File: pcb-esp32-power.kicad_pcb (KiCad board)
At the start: 2 copper layers, 48.6 x 47.4 mm, 35 parts, among them IC1 IP5108, IC2 SY8008B, J1 C-OBD-II-16M, J2 Conn_01x02, J3 Bus_Connector, U1 STEPDOWN12_5

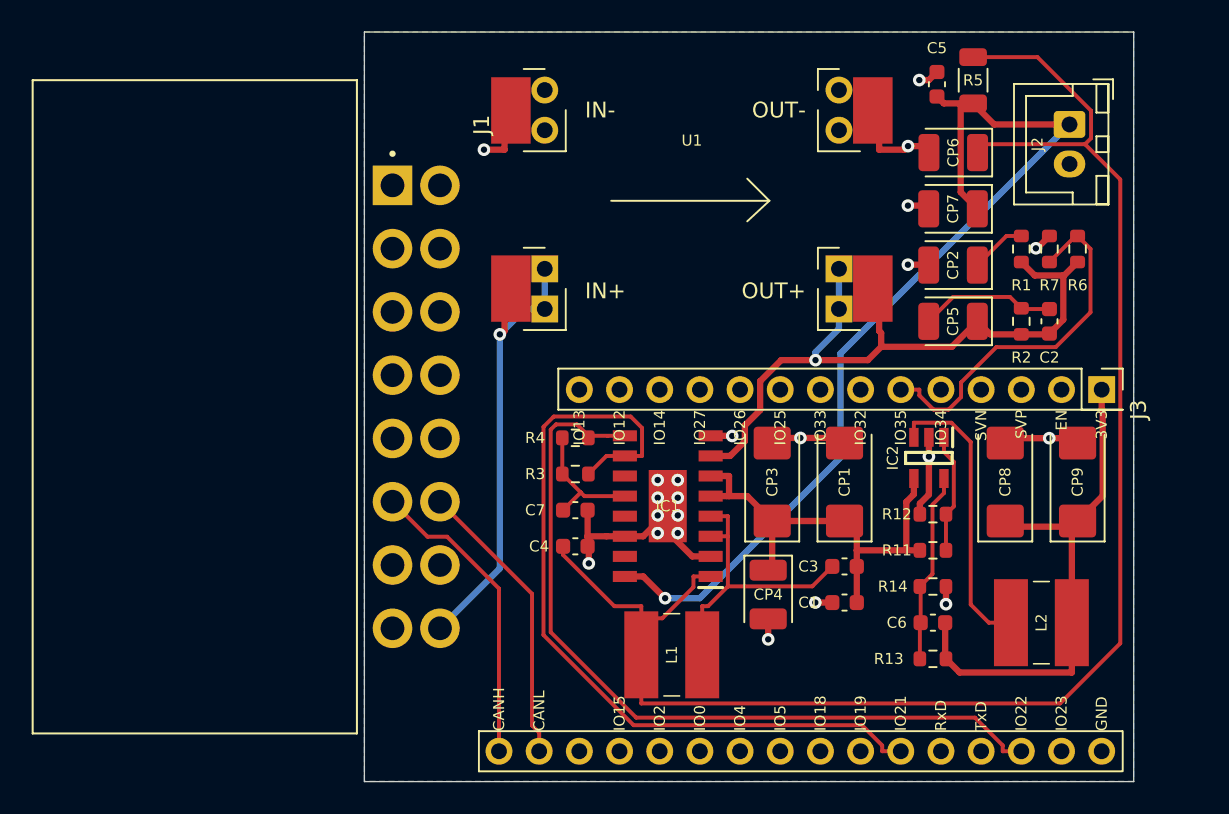
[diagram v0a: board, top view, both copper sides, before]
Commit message: Footprints für "Hand solder"
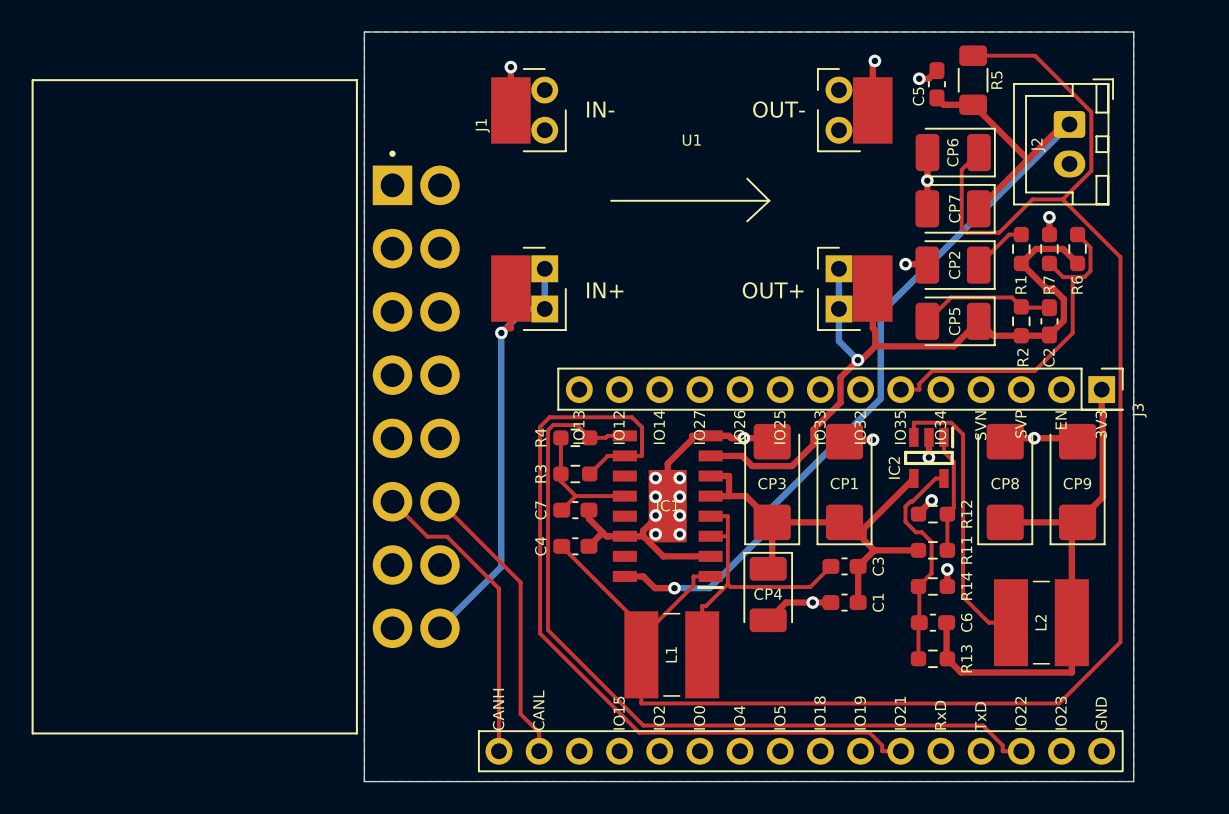
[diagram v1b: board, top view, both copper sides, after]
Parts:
- C1, C2, C3, C4, C5, C6, C7: footprint Capacitor_SMD:C_0603_1608Metric -> Capacitor_SMD:C_0603_1608Metric_Pad1.08x0.95mm_HandSolder
- CP1, CP3, CP8, CP9: footprint Capacitor_Tantalum_SMD:CP_EIA-6032-28_Kemet-C -> Capacitor_Tantalum_SMD:CP_EIA-6032-28_Kemet-C_Pad2.25x2.35mm_HandSolder
- CP2, CP4, CP5, CP6, CP7: footprint Capacitor_Tantalum_SMD:CP_EIA-3528-21_Kemet-B -> Capacitor_Tantalum_SMD:CP_EIA-3528-21_Kemet-B_Pad1.50x2.35mm_HandSolder
- R1, R11, R12, R13, R14, R2, R3, R4, R6, R7: footprint Resistor_SMD:R_0603_1608Metric -> Resistor_SMD:R_0603_1608Metric_Pad0.98x0.95mm_HandSolder
- R5: footprint Resistor_SMD:R_1206_3216Metric -> Resistor_SMD:R_1206_3216Metric_Pad1.30x1.75mm_HandSolder
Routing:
- net Net-(C4-Pad1): track 101.3 -> 107.3 mm
- net GND: track 48.3 -> 51.2 mm, vias 22 -> 21
- net 5VIN: track 45.2 -> 47.9 mm
- net Net-(C6-Pad2): track 12.1 -> 14.1 mm
- net EXTPOW: track 23.4 -> 21.9 mm
- net +BATT: track 61.2 -> 59.7 mm
- net +12V: track 29.1 -> 29.7 mm

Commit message: Mit SY8008
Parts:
- removed C1, C4, C5: 104, Capacitor_SMD:C_0603_1608Metric_Pad1.08x0.95mm_HandSolder
- removed C6: 47pF, Capacitor_SMD:C_0603_1608Metric_Pad1.08x0.95mm_HandSolder
- removed C7: 2.2uF, Capacitor_SMD:C_0603_1608Metric_Pad1.08x0.95mm_HandSolder
- removed CP6, CP7: 10uF, Capacitor_Tantalum_SMD:CP_EIA-3528-21_Kemet-B_Pad1.50x2.35mm_HandSolder
- removed CP8, CP9: 22uF, Capacitor_Tantalum_SMD:CP_EIA-6032-28_Kemet-C_Pad2.25x2.35mm_HandSolder
- removed L2: 2.2uH, IP5108:CD54_Inductor
- removed the R1 at (167.9, 100.3)
- removed R11, R12: 100k, Resistor_SMD:R_0603_1608Metric_Pad0.98x0.95mm_HandSolder
- removed R13: 453k 1%, Resistor_SMD:R_0603_1608Metric_Pad0.98x0.95mm_HandSolder
- removed R14: 100k 1%, Resistor_SMD:R_0603_1608Metric_Pad0.98x0.95mm_HandSolder
- removed the R2 at (167.9, 104.9)
- added D1: B5819W, Diode_SMD:D_SOD-123, F.Cu at (157.2, 117.6)
- added Q1: Si2307BDS, Package_TO_SOT_SMD:SOT-23, F.Cu at (157.2, 114.0)
- added R10: 100k 1%, Resistor_SMD:R_0603_1608Metric_Pad0.98x0.95mm_HandSolder, F.Cu at (162.6, 122.7)
- added R6: 10K, Resistor_SMD:R_0603_1608Metric_Pad0.98x0.95mm_HandSolder, F.Cu at (157.7, 127.3)
- added R7: 100k, Resistor_SMD:R_0603_1608Metric_Pad0.98x0.95mm_HandSolder, F.Cu at (162.6, 120.4)
- added R8: 100k, Resistor_SMD:R_0603_1608Metric_Pad0.98x0.95mm_HandSolder, F.Cu at (162.6, 118.1)
- added R9: 453k 1%, Resistor_SMD:R_0603_1608Metric_Pad0.98x0.95mm_HandSolder, F.Cu at (162.6, 127.3)
- C2: value 104 -> 100nF
- C3: value 4.7nF -> 47pF
- CP2, CP5: value 10uF -> 22uF; footprint Capacitor_Tantalum_SMD:CP_EIA-3528-21_Kemet-B_Pad1.50x2.35mm_HandSolder -> Capacitor_Tantalum_SMD:CP_EIA-6032-28_Kemet-C_Pad2.25x2.35mm_HandSolder
- CP3: value 22uF -> 10uF; footprint Capacitor_Tantalum_SMD:CP_EIA-6032-28_Kemet-C_Pad2.25x2.35mm_HandSolder -> Capacitor_Tantalum_SMD:CP_EIA-3528-21_Kemet-B_Pad1.50x2.35mm_HandSolder
- IC1: value IP5108 -> TP4054-42-SOT25-R; footprint IP5108:IP5108 -> tp4054:SOT95P280X100-5N
- L1: value 1uH -> 2.2uH
- R1: renamed from R6; value R -> 200k
- R2: renamed from R7; value R -> 390k
- R3, R4: value 3.3k -> 470k
- R5: value 10mOhm -> 2K; footprint Resistor_SMD:R_1206_3216Metric_Pad1.30x1.75mm_HandSolder -> Resistor_SMD:R_0603_1608Metric_Pad0.98x0.95mm_HandSolder
- moved IC1 30.7 mm to (171.7, 100.6), turned to 270 degrees
- moved R4 26.1 mm to (164.8, 105.2), turned to 90 degrees
- moved CP4 25.9 mm to (163.6, 99.1), turned to 90 degrees
- moved CP3 25.3 mm to (163.6, 92.5), turned to 270 degrees
- moved R3 25.0 mm to (162.8, 105.2), turned to 270 degrees
- moved L1 23.9 mm to (169.7, 124.2), turned to 270 degrees
- moved C2 23.3 mm to (157.7, 125.0), turned to 180 degrees
- moved CP5 18.3 mm to (155.7, 121.4)
- moved R5 17.5 mm to (173.0, 105.2), turned to 270 degrees
- moved CP2 16.9 mm to (172.0, 116.1), turned to 90 degrees
- moved CP1 11.0 mm to (167.6, 116.1)
- moved C3 7.42 mm to (162.6, 125.0)
- moved R2 5.58 mm to (166.9, 105.2)
- moved R1 5.45 mm to (168.9, 105.2), turned to 270 degrees
- moved IC2 0.92 mm to (162.6, 114.3)
- renumbered J3 to J2, J2 to J3
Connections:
- C2 pad 1: 5VIN -> 5VOUT
- C2 pad 2: Net-(C2-Pad2) -> GND
- C3 pad 1: 5VOUT -> +3V3
- CP1 pad 1: 5VOUT -> +3V3
- CP2 pad 1: Net-(CP2-Pad1) -> +3V3
- CP3 pad 1: 5VOUT -> +BATT
- CP4 pad 1: 5VOUT -> 5VIN
- CP5 pad 1: 5VIN -> 5VOUT
- CP5 pad 2: Net-(C2-Pad2) -> GND
- IC1 pad 1: Net-(C4-Pad1) -> Net-(IC1-Pad1)
- IC1 pad 3: Net-(C3-Pad2) -> +BATT
- IC1 pad 4: Net-(C3-Pad2) -> 5VIN
- IC1 pad 5: 5VOUT -> Net-(IC1-Pad5)
- IC2 pad 5: Net-(C6-Pad2) -> Net-(C3-Pad2)
- J2 pad 5: Net-(J3-Pad5) -> EXTPOW
- J2 pad 6: EXTPOW -> BATTVOLT
- L1 pad 1: Net-(C4-Pad1) -> +3V3
- L1 pad 2: Net-(C3-Pad2) -> Net-(IC2-Pad3)
- R3 pad 1: Net-(C7-Pad1) -> +BATT
- R3 pad 2: SDA -> BATTVOLT
- R4 pad 1: Net-(C7-Pad1) -> BATTVOLT
- R4 pad 2: SCL -> GND
- R5 pad 1: +BATT -> Net-(IC1-Pad5)
- R5 pad 2: Net-(C4-Pad1) -> GND
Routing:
- net Net-(C4-Pad1): track 107.3 -> 0.00 mm
- net SDA: track 51.7 -> 0.00 mm
- net SCL: track 51.3 -> 0.00 mm
- net GND: track 51.2 -> 29.5 mm, vias 21 -> 10
- net EXTPOW: track 21.9 -> 7.62 mm
- net Net-(C6-Pad2): track 14.1 -> 0.00 mm
- net +BATT: track 59.7 -> 46.3 mm, vias 1 -> 0
- net 5VOUT: track 28.7 -> 17.9 mm
- net Net-(C2-Pad2): track 8.61 -> 0.00 mm
- net Net-(C7-Pad1): track 8.43 -> 0.00 mm
- net BATTVOLT: track 0.00 -> 6.57 mm
- net Net-(C3-Pad2): track 18.9 -> 12.5 mm
- net Net-(CP2-Pad1): track 3.49 -> 0.00 mm
- net Net-(IC1-Pad5): track 0.00 -> 2.49 mm
- net 5VIN: track 47.9 -> 45.6 mm, vias 1 -> 0
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
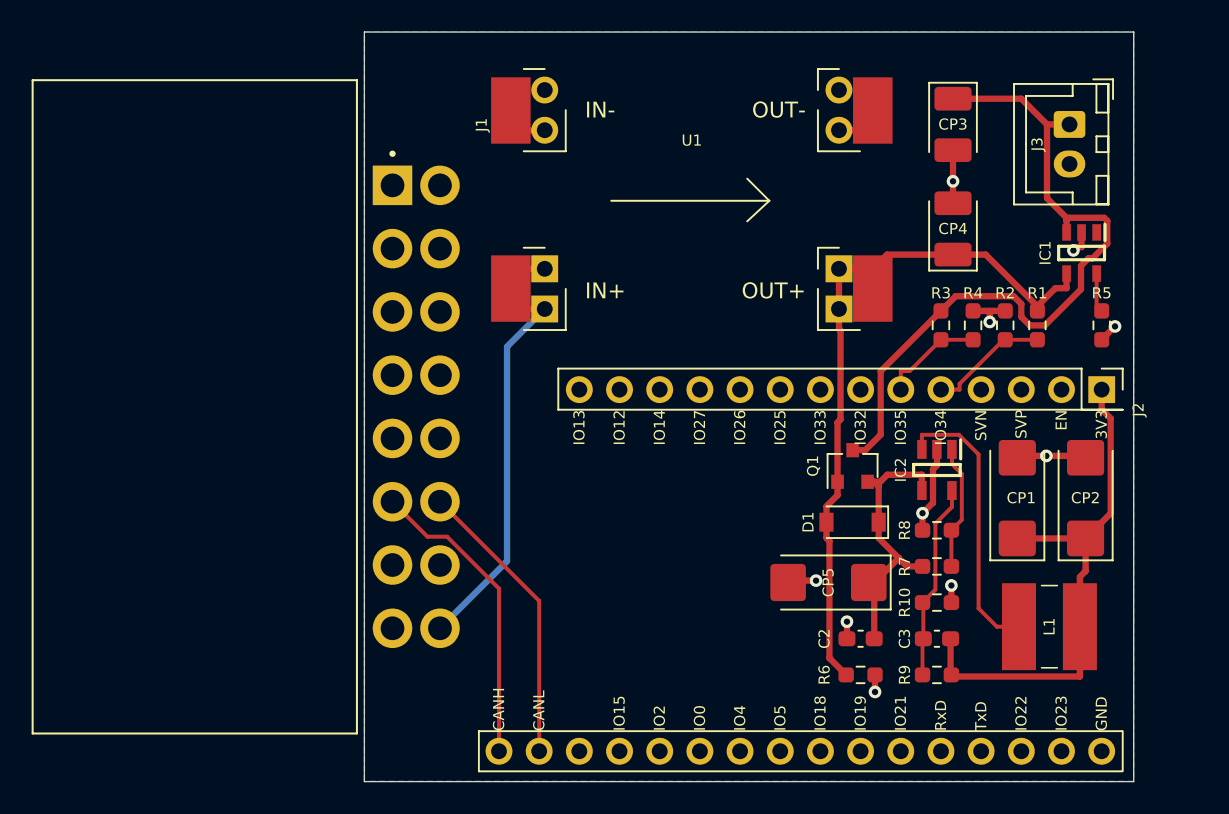
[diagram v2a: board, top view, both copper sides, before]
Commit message: Mit Sy8008 und LTC3530
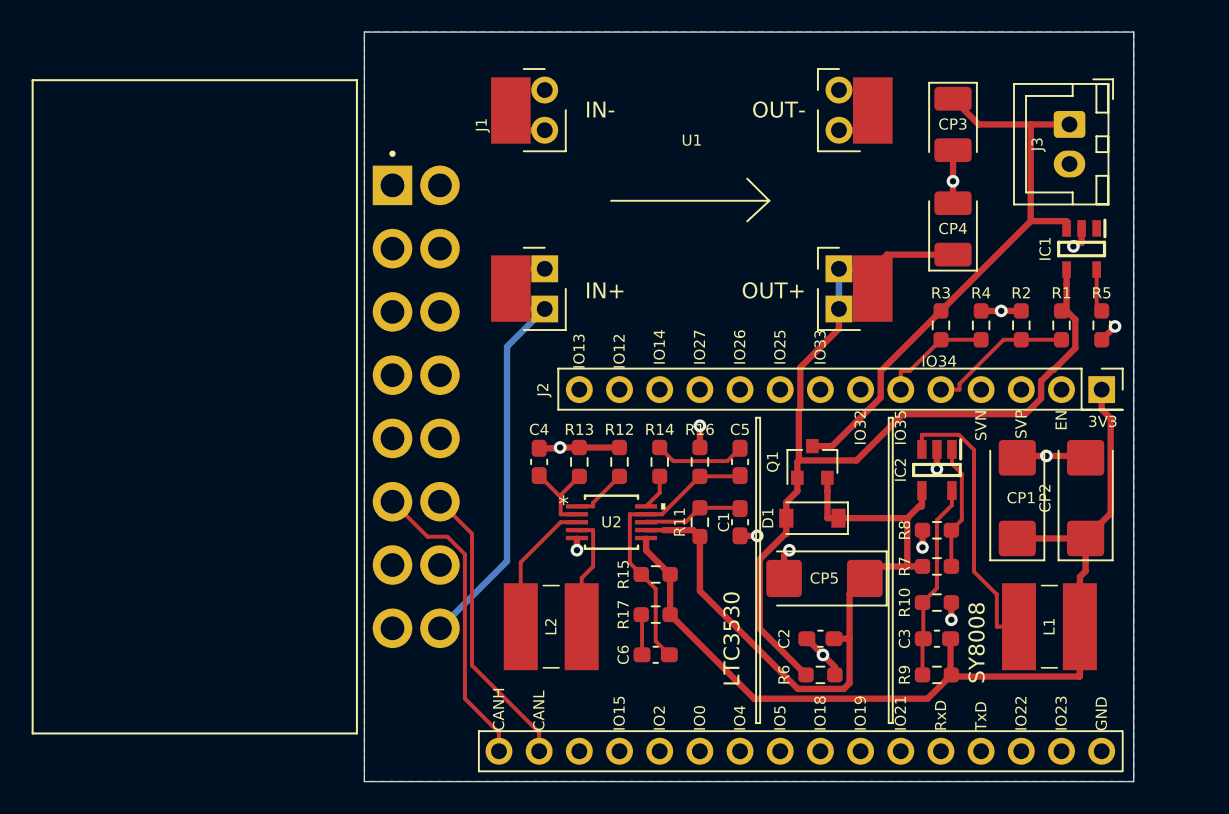
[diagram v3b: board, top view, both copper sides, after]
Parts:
- added C1: 10nF, Capacitor_SMD:C_0603_1608Metric_Pad1.08x0.95mm_HandSolder, F.Cu at (150.1, 117.6)
- added C4: 10nF, Capacitor_SMD:C_0603_1608Metric_Pad1.08x0.95mm_HandSolder, F.Cu at (137.4, 113.8)
- added C5: 560pF, Capacitor_SMD:C_0603_1608Metric_Pad1.08x0.95mm_HandSolder, F.Cu at (150.1, 113.8)
- added C6: 33pF, Capacitor_SMD:C_0603_1608Metric_Pad1.08x0.95mm_HandSolder, F.Cu at (144.8, 126.0)
- added L2: 4.7uH, ltc3530:CD54_Inductor, F.Cu at (138.2, 124.2)
- added R11: 1M, Resistor_SMD:R_0603_1608Metric_Pad0.98x0.95mm_HandSolder, F.Cu at (147.6, 117.6)
- added R12: 33.2k, Resistor_SMD:R_0603_1608Metric_Pad0.98x0.95mm_HandSolder, F.Cu at (142.5, 113.8)
- added R13: 200k, Resistor_SMD:R_0603_1608Metric_Pad0.98x0.95mm_HandSolder, F.Cu at (140.0, 113.8)
- added R14: 10k, Resistor_SMD:R_0603_1608Metric_Pad0.98x0.95mm_HandSolder, F.Cu at (145.0, 113.8)
- added R15: 1M, Resistor_SMD:R_0603_1608Metric_Pad0.98x0.95mm_HandSolder, F.Cu at (144.8, 120.9)
- added R16: 576k, Resistor_SMD:R_0603_1608Metric_Pad0.98x0.95mm_HandSolder, F.Cu at (147.6, 113.8)
- added R17: 15k, Resistor_SMD:R_0603_1608Metric_Pad0.98x0.95mm_HandSolder, F.Cu at (144.8, 123.4)
- added U2: LTC3530EMS, ltc3530:MSOP-10_MS, F.Cu at (142.0, 117.6)
- moved D1 2.55 mm to (154.7, 117.3)
- moved Q1 2.55 mm to (154.7, 113.8)
- moved C2 2.54 mm to (155.2, 125.0)
- moved R6 2.54 mm to (155.2, 127.3)
- moved R1 1.52 mm to (170.4, 105.2)
- moved R2 1.02 mm to (167.9, 105.2)
- moved R4 0.51 mm to (165.4, 105.2)
- moved CP5 0.36 mm to (155.4, 121.2)
- moved IC1 0.25 mm to (171.7, 100.3)
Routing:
- net 5VOUT: track 17.9 -> 44.0 mm
- net +3V3: track 34.0 -> 60.0 mm
- net 5VIN: track 45.6 -> 64.4 mm
- net Net-(C5-Pad1): track 0.00 -> 17.9 mm
- net +BATT: track 46.3 -> 37.6 mm
- net Net-(L2-Pad2): track 0.00 -> 8.67 mm
- net Net-(L2-Pad1): track 0.00 -> 7.43 mm
- net Net-(C1-Pad1): track 0.00 -> 6.34 mm
- net GND: track 29.5 -> 35.5 mm, vias 10 -> 14
- net Net-(C4-Pad1): track 0.00 -> 5.78 mm
- net Net-(C5-Pad2): track 0.00 -> 5.77 mm
- net Net-(R12-Pad1): track 0.00 -> 3.61 mm
- net Net-(C6-Pad1): track 0.00 -> 2.56 mm
- net Net-(R14-Pad2): track 0.00 -> 2.25 mm
- net EXTPOW: track 7.62 -> 9.14 mm
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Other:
- board text added: "LTC3530"
- board text added: "SY8008"

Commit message: LED zugefügt
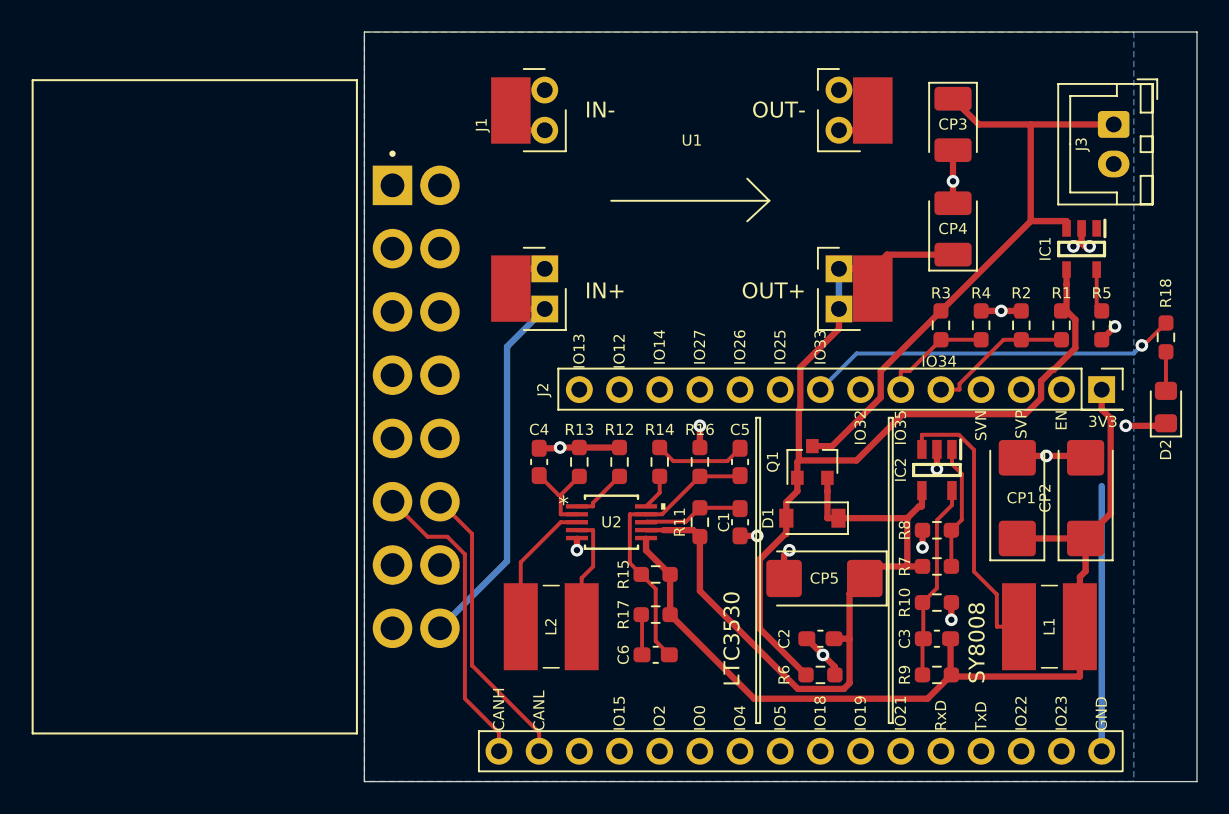
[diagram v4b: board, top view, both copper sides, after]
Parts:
- added D2: LED green, LED_SMD:LED_0805_2012Metric_Pad1.15x1.40mm_HandSolder, F.Cu at (177.0, 110.3)
- added R18: 1K, Resistor_SMD:R_0603_1608Metric_Pad0.98x0.95mm_HandSolder, F.Cu at (177.0, 105.9)
- moved J3 2.79 mm to (173.7, 92.5)
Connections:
- J2 pad 8: Net-(J2-Pad8) -> LED
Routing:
- net LED: track 0.00 -> 23.6 mm, vias 0 -> 1
- net GND: track 35.5 -> 55.4 mm, vias 14 -> 16
- net +BATT: track 37.6 -> 40.3 mm
- net Net-(D2-Pad2): track 0.00 -> 2.47 mm
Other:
- board size 48.6 x 47.4 mm -> 52.6 x 47.4 mm
